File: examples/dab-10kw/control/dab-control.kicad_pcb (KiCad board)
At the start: 4 copper layers, 160 x 120 mm, 224 parts, among them J1 controlCARD HSEC8 180-contact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, J2 PRIMARY POWER BOARD harness, J3 SECONDARY POWER BOARD harness, J4 12 V AUXILIARY IN, J5 CAN BUS, J6 RS-485, J7 JTAG 14-pin, J8 MANUAL RESET, U1 TPS26400PWPR, U10 SN74LV21APWR, U11 SN74LV21APWR, U12 SN74LV21APWR, U13 SN74LV04APWR, U14 REF3130AIDBZR, U15 TLV1702AIDGKR, U16 SN74LVC1G74DCTR, U17 SN74LVC2G08DCTR, U18 OPA4192IPWR, U19 TCAN1042HGVDRQ1, U2 TPS54302DDCR, U20 THVD1450DR, U3 TPS7A2033PDBVR, U4 TPS3808G01DBVR, U5 SN74LVC2G08DCTR, U6 SN74LVC2G08DCTR, U7 SN74LVC2G08DCTR, U8 SN74LVC2G08DCTR, U9 SN74LV21APWR

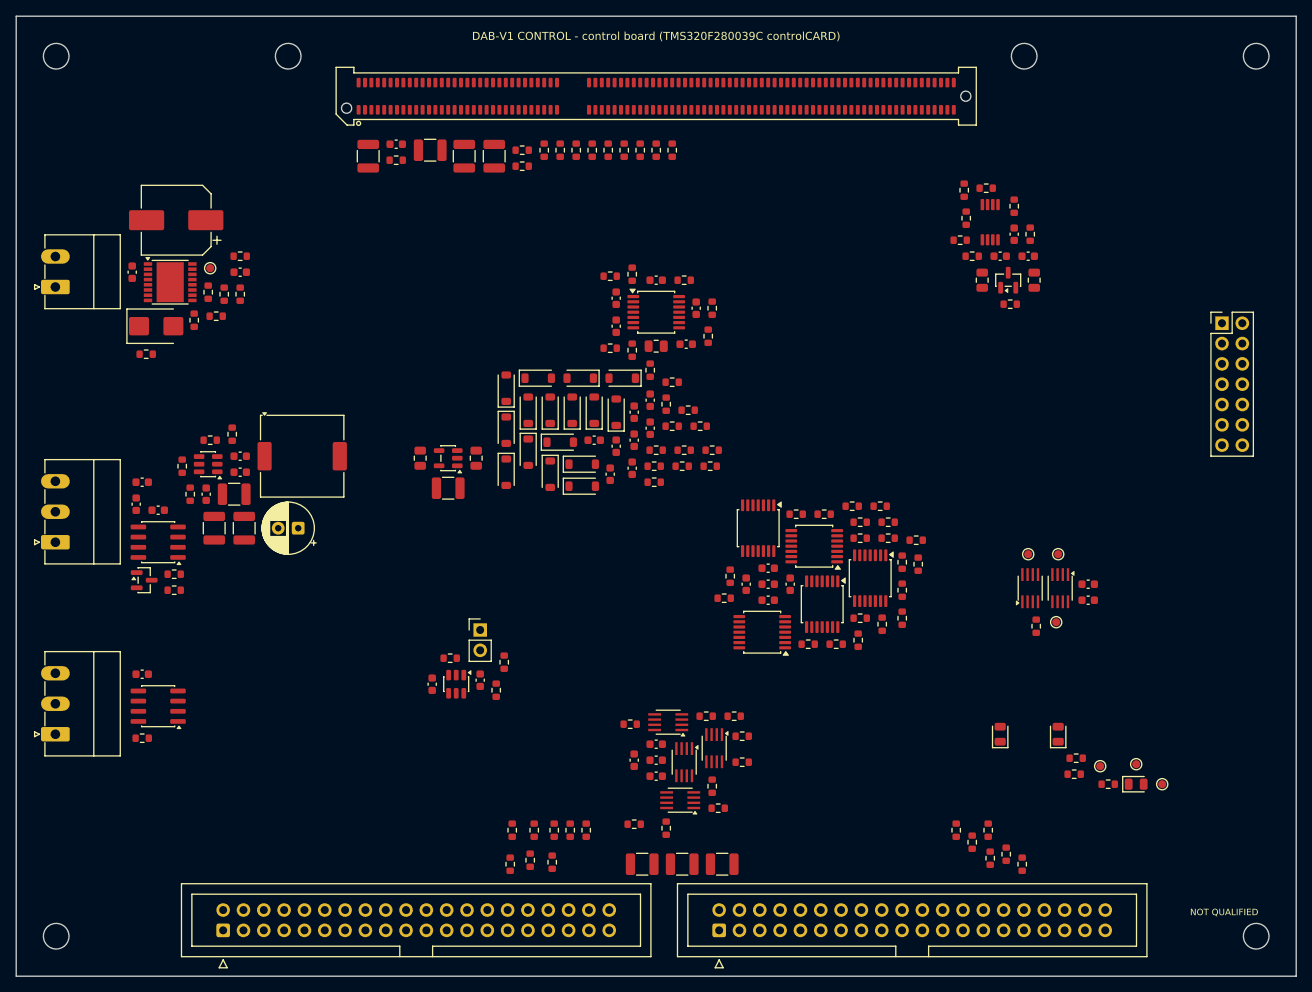
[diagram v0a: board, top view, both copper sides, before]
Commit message: Remediate DAB-V1 routing: fine-pitch row escapes, exit lanes, plane continuity, time-boxed router
Root causes of the 2026-10-21 DRC failures and open connections of the three DAB-V1 boards are documented in
docs/dab-10kw/routing-remediation.md; the generator and the grid router were changed accordingly and the boards were
regenerated and re-verified with kicad-cli 10.0.6 (ERC, DRC --schematic-parity --severity-all --refill-zones, exports,
netlist equality, copper islands, barrier geometry).

Results (before -> after): primary 22 DRC errors -> 0, 82 unconnected -> 26; secondary 2 -> 0, 81 -> 23;
control not routed (499) -> routed, 0 errors, 24 unconnected. ERC 0 and parity 0 on all boards. Open connections
remain, so no board is manufacturing-ready.

Generator: fine-pitch row escapes (automation/dab_v1/fanout_rows.py: same-net bridges, one stub per run, computed stub
lengths, exit lanes), placement fan-out band and part gap, DESAT diode out of the plane band, sense pours joined to
the planes, AC_B riser over J4 capped at the Hall bars, 0.5 mm module input rails. Router: footprint copper graphics
as via exclusions, geometric stub-end acceptance, exit lanes at stub width (critical pads included), stranded ground
routing, time_budget_s with checkpoints. Tests added; KiCad-dependent tests gated for CI; pyproject 0.1.0; README in
the AIPE template (former README moved to docs/history.md).

Co-Authored-By: Claude Fable 5.1 <noreply@anthropic.com>
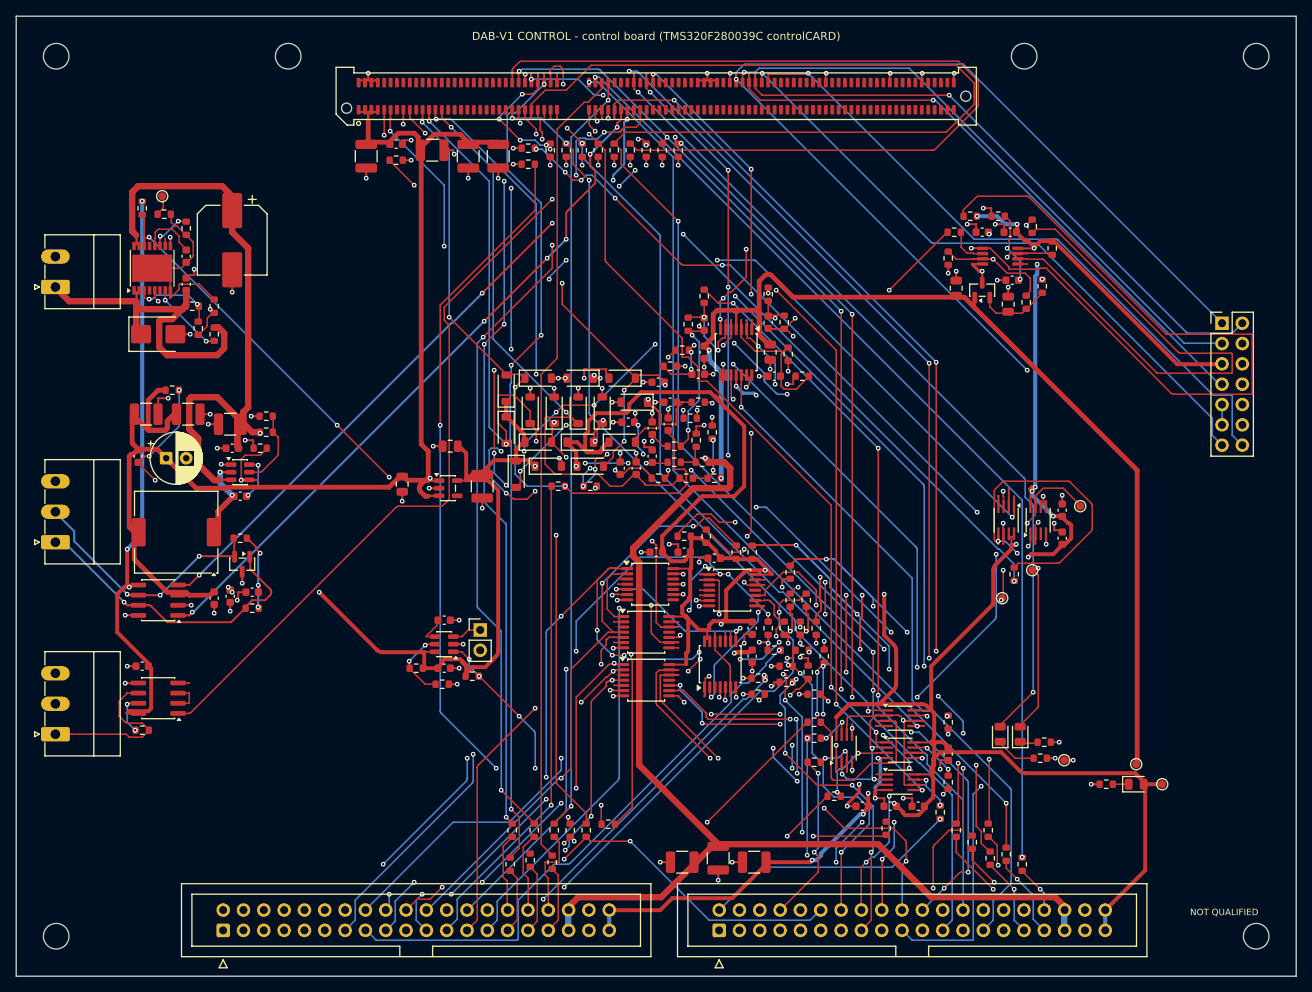
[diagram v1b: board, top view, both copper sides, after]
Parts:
- moved R29 40.4 mm to (116.5, 95.8), turned to -90 degrees
- moved C24 39.3 mm to (116.5, 92.2), turned to -90 degrees
- moved C23 33.7 mm to (112.8, 98.8), turned to 180 degrees
- moved R27 30.6 mm to (116.5, 88.2)
- moved C21 29.5 mm to (109.2, 98.8), turned to 180 degrees
- moved U6 29.2 mm to (110.5, 91.8), turned to 0 degrees
- moved U5 27.6 mm to (110.5, 87.8), turned to 0 degrees
- moved C22 26.4 mm to (105.8, 98.8), turned to 180 degrees
- moved R31 25.5 mm to (115.5, 99.5), turned to -90 degrees
- moved R42 25.0 mm to (92.8, 84.8)
- moved U7 23.6 mm to (110.5, 95.8), turned to 0 degrees
- moved R65 22.5 mm to (96.0, 38.2), turned to 90 degrees
- moved U11 22.3 mm to (78.8, 77.0), turned to 0 degrees
- moved R40 22.1 mm to (92.8, 82.8)
- moved R45 22.1 mm to (96.2, 83.2)
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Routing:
- net 3V3: track 0.00 -> 628.7 mm, vias 0 -> 25
- net 5V0: track 0.00 -> 338.9 mm, vias 0 -> 3
- net 12V_E: track 0.00 -> 274.6 mm, vias 0 -> 2
- net GND_CTRL: track 0.00 -> 209.0 mm, vias 0 -> 131
- net EPWM2B: track 0.00 -> 204.5 mm, vias 0 -> 3
- net OV_P_OK: track 0.00 -> 165.4 mm, vias 0 -> 2
- net TEMP_PWM_S_BH: track 0.00 -> 147.6 mm, vias 0 -> 5
- net S_RDY_BH: track 0.00 -> 143.6 mm, vias 0 -> 5
- net S_OC_TRIP_N: track 0.00 -> 130.9 mm, vias 0 -> 9
- net SDFM_S_D: track 0.00 -> 120.5 mm, vias 0 -> 2
- net SDFM_S_CLK: track 0.00 -> 117.9 mm, vias 0 -> 2
- net TEMP_PWM_S_BL: track 0.00 -> 117.0 mm, vias 0 -> 4
- net EPWM3B: track 0.00 -> 115.8 mm, vias 0 -> 6
- net EPWM4A: track 0.00 -> 114.9 mm, vias 0 -> 5
- net S_RDY_AH: track 0.00 -> 113.5 mm, vias 0 -> 8
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- added copper zone on In1.Cu, net GND_CTRL
